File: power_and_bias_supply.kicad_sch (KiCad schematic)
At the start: 35 parts, among them Q501 2N7002, U501 MCP6L02x-xSN, U502 LM2733YMFX/NOPB, U503 TPS22944DCKR, X5 Conn_Coaxial

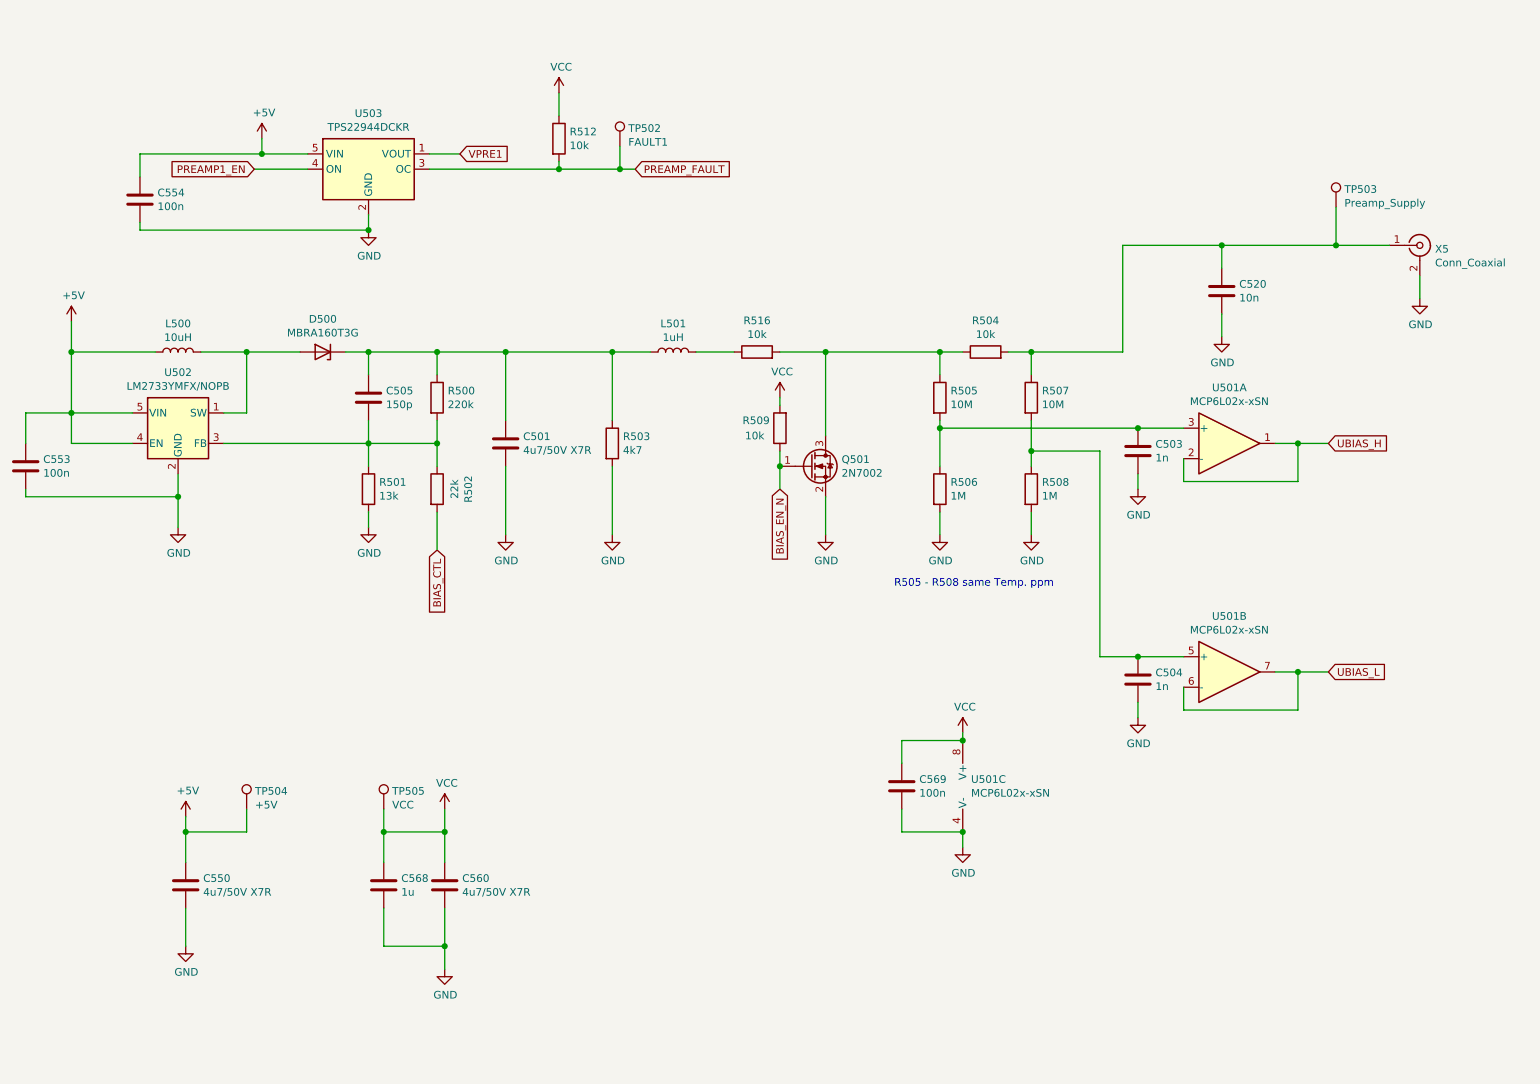
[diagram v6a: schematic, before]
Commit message: Progress in PCB. Some changes in Schematis. Solderjumper for modular design added.
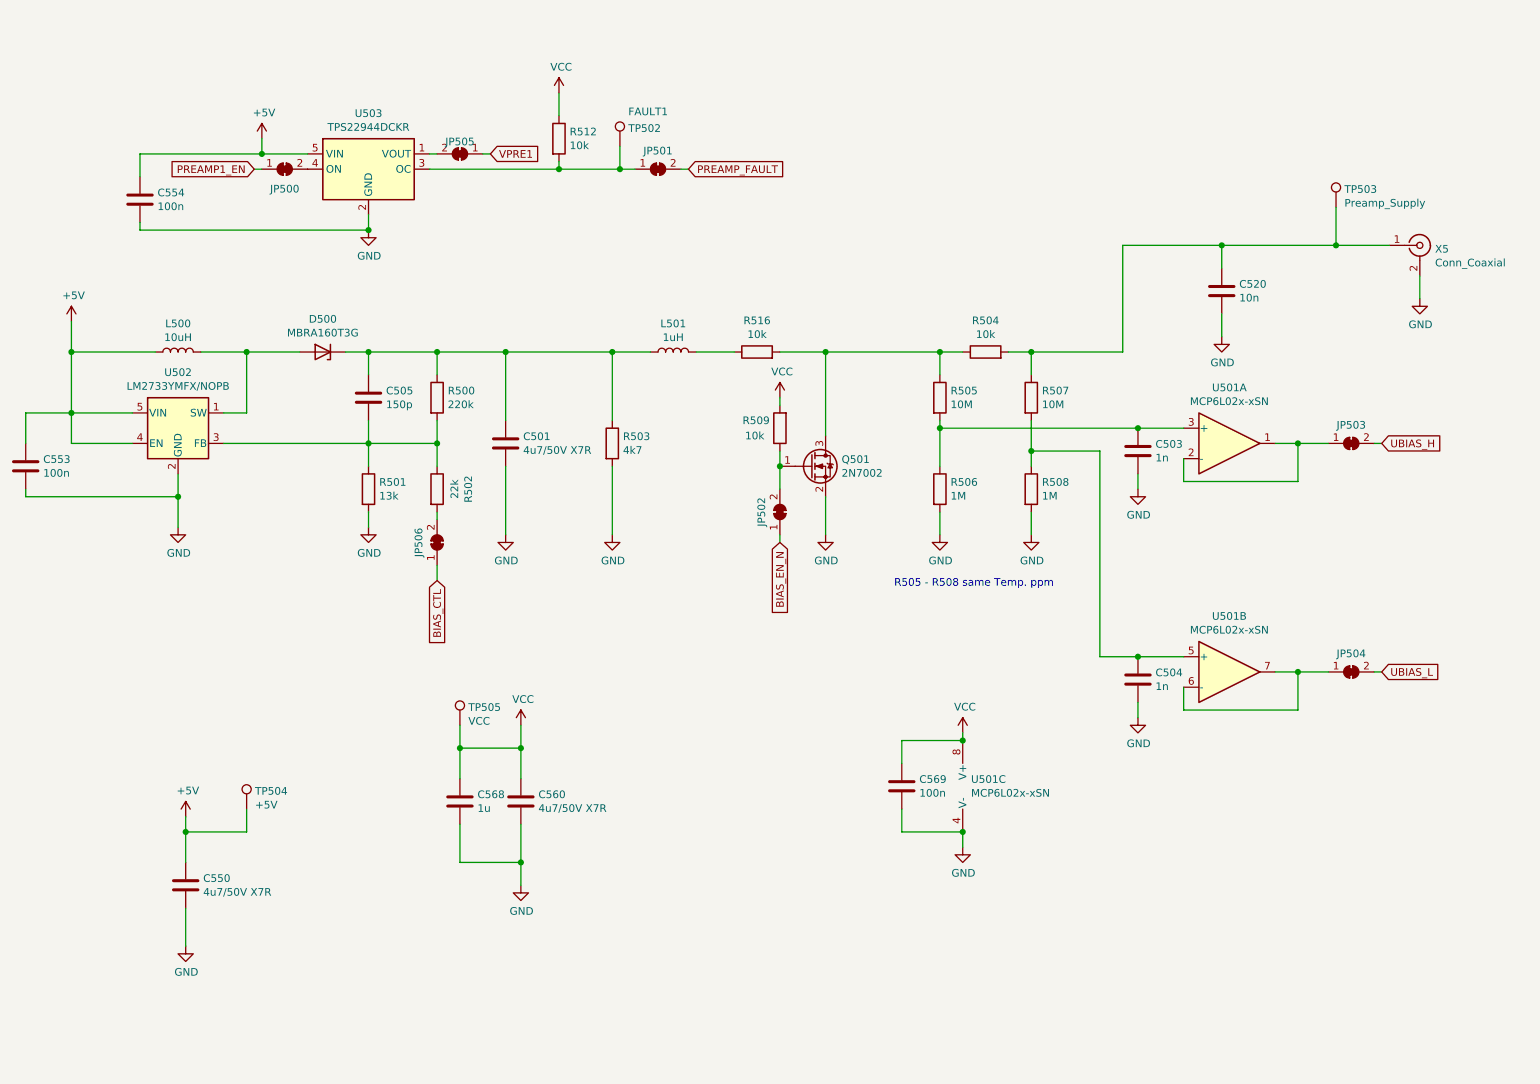
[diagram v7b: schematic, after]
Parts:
- added JP500, JP501, JP502, JP503, JP504, JP505, JP506: SolderJumper_2_Bridged, Jumper:SolderJumper-2_P1.3mm_Bridged_Pad1.0x1.5mm, symbol Jumper:SolderJumper_2_Bridged
- X5: footprint muonpi-kicad-library:SMA_Samtec_SMA-J-P-X-ST-EM1_EdgeMount -> muonpi-kicad-library:Connector_Coaxial_SMA_edge_combined
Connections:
- net BIAS_CTL: now also JP506.1 (A); no longer R502.2
- net BIAS_EN_N: now also JP502.1 (A); no longer Q501.1 (G), R509.1
- net PREAMP1_EN: now also JP500.1 (A); no longer U503.4 (ON)
- net PREAMP_FAULT: now also JP501.2 (B); no longer R512.2, TP502.1, U503.3 (OC)
- net UBIAS_H: now also JP503.2 (B); no longer U501.1, U501.2 (-)
- net UBIAS_L: now also JP504.2 (B); no longer U501.6 (-), U501.7
- net VPRE1: now also JP505.1 (A); no longer U503.1 (VOUT)
- new net: JP501.1 (A), R512.2, TP502.1, U503.3 (OC)
- new net: JP500.2 (B), U503.4 (ON)
- new net: JP503.1 (A), U501.1, U501.2 (-)
- new net: JP505.2 (B), U503.1 (VOUT)
- new net: JP506.2 (B), R502.2
- new net: JP502.2 (B), Q501.1 (G), R509.1
- new net: JP504.1 (A), U501.6 (-), U501.7
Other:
- moved on the sheet: C560, C568, TP505

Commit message: Notes added in Schematics. Vias added on PCB.
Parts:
- TP503: value Preamp_Supply -> BIAS_Supply
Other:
- note added: "Preamp Supply Voltage"
- moved on the sheet: JP505
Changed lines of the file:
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@@
     (stroke (width 0) (type solid) (color 0 0 0 0))
   )
-  (wire (pts (xy 88.9 39.37) (xy 90.17 39.37))
+  (wire (pts (xy 88.9 39.37) (xy 93.98 39.37))
     (stroke (width 0) (type solid) (color 0 0 0 0))
   )
@@
     (stroke (width 0) (type solid) (color 0 0 0 0))
   )
+  (wire (pts (xy 93.98 19.05) (xy 130.81 19.05))
+    (stroke (width 0) (type solid) (color 0 0 0 0))
+  )
+  (wire (pts (xy 93.98 39.37) (xy 93.98 19.05))
+    (stroke (width 0) (type solid) (color 0 0 0 0))
+  )
   (wire (pts (xy 93.98 134.62) (xy 93.98 138.43))
     (stroke (width 0) (type solid) (color 0 0 0 0))
@@
     (stroke (width 0) (type solid) (color 0 0 0 0))
   )
-  (wire (pts (xy 97.79 39.37) (xy 99.06 39.37))
-    (stroke (width 0) (type solid) (color 0 0 0 0))
-  )
   (wire (pts (xy 101.6 72.39) (xy 101.6 83.82))
     (stroke (width 0) (type solid) (color 0 0 0 0))
@@
     (stroke (width 0) (type solid) (color 0 0 0 0))
   )
+  (wire (pts (xy 138.43 19.05) (xy 139.7 19.05))
+    (stroke (width 0) (type solid) (color 0 0 0 0))
+  )
   (wire (pts (xy 147.32 80.01) (xy 147.32 81.28))
     (stroke (width 0) (type solid) (color 0 0 0 0))
@@
   (wire (pts (xy 254 59.69) (xy 254 63.5))
     (stroke (width 0) (type solid) (color 0 0 0 0))
+  )
+  (text "Preamp Supply Voltage" (at 139.7 24.13 0)
+    (effects (font (size 1.27 1.27)) (justify left bottom))
   )
   (text "R505 - R508 same Temp. ppm" (at 166.37 111.76 0)
@@
     )
   )
-  (global_label "VPRE1" (shape input) (at 99.06 39.37 0)
-    (effects (font (size 1.27 1.27)) (justify left))
-    (property "Intersheet References" "${INTERSHEET_REFS}" (id 0) (at 108.9842 39.2906 0)
-      (effects (font (size 1.27 1.27)) (justify left) hide)
-    )
-  )
   (global_label "PREAMP_FAULT" (shape input) (at 132.08 41.91 0)
     (effects (font (size 1.27 1.27)) (justify left))
@@
     )
   )
+  (global_label "VPRE1" (shape input) (at 139.7 19.05 0)
+    (effects (font (size 1.27 1.27)) (justify left))
+    (property "Intersheet References" "${INTERSHEET_REFS}" (id 0) (at 149.6242 18.9706 0)
+      (effects (font (size 1.27 1.27)) (justify left) hide)
+    )
+  )
   (global_label "BIAS_EN_N" (shape input) (at 147.32 104.14 270)
     (effects (font (size 1.27 1.27)) (justify right))
@@
       (effects (font (size 1.27 1.27)) (justify left))
     )
-    (property "Value" "Preamp_Supply" (id 1) (at 241.4271 47.5678 0)
+    (property "Value" "BIAS_Supply" (id 1) (at 241.4271 47.5678 0)
       (effects (font (size 1.27 1.27)) (justify left))
     )
@@
     (pin "2")
   )
-  (symbol (lib_id "Jumper:SolderJumper_2_Bridged") (at 93.98 39.37 180) (unit 1)
-    (in_bom no) (on_board yes)
-    (property "Reference" "JP505" (id 0) (at 93.98 37.3422 0))
-    (property "Value" "SolderJumper_2_Bridged" (id 1) (at 93.98 41.3935 0)
-      (effects (font (size 1.27 1.27)) hide)
-    )
-    (property "Footprint" "Jumper:SolderJumper-2_P1.3mm_Bridged_Pad1.0x1.5mm" (id 2) (at 93.98 39.37 0)
-      (effects (font (size 1.27 1.27)) hide)
-    )
-    (property "Datasheet" "~" (id 3) (at 93.98 39.37 0)
-      (effects (font (size 1.27 1.27)) hide)
-    )
-    (pin "1")
-    (pin "2")
-  )
   (symbol (lib_id "Jumper:SolderJumper_2_Bridged") (at 127 41.91 0) (unit 1)
     (in_bom no) (on_board yes)
@@
       (effects (font (size 1.27 1.27)) hide)
     )
+    (pin "1")
+    (pin "2")
+  )
+  (symbol (lib_id "Jumper:SolderJumper_2_Bridged") (at 134.62 19.05 180) (unit 1)
+    (in_bom no) (on_board yes)
+    (property "Reference" "JP505" (id 0) (at 134.62 17.0222 0))
+    (property "Value" "SolderJumper_2_Bridged" (id 1) (at 134.62 21.0735 0)
+      (effects (font (size 1.27 1.27)) hide)
+    )
+    (property "Footprint" "Jumper:SolderJumper-2_P1.3mm_Bridged_Pad1.0x1.5mm" (id 2) (at 134.62 19.05 0)
+      (effects (font (size 1.27 1.27)) hide)
+    )
+    (property "Datasheet" "~" (id 3) (at 134.62 19.05 0)
+      (effects (font (size 1.27 1.27)) hide)
+    )
